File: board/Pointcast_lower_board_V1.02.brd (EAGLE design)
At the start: 100.3 x 80 mm, 29 parts, among them U6 Ethernet, X2 3G module, X4 3GS shield

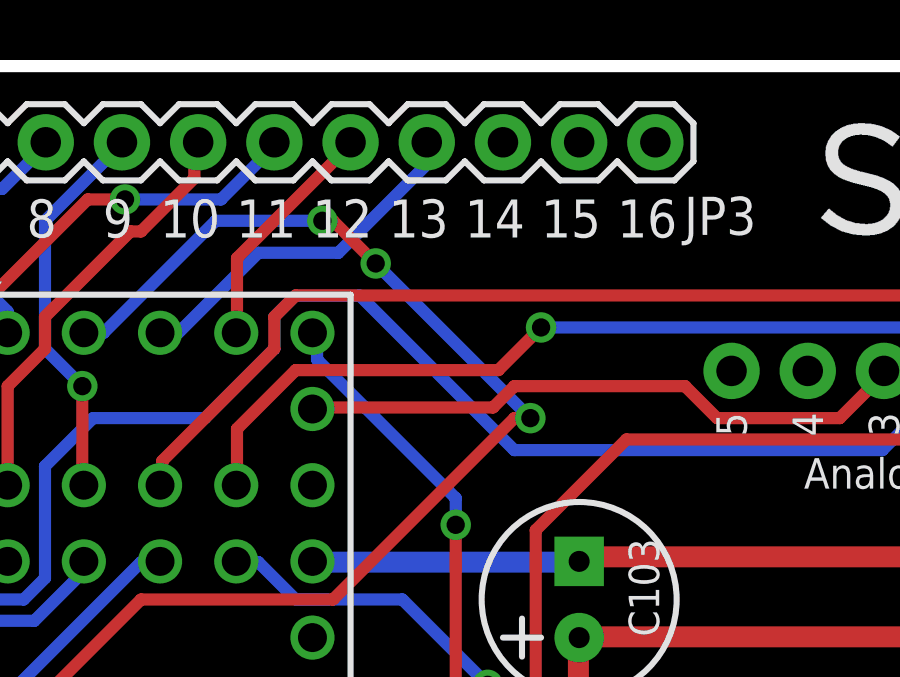
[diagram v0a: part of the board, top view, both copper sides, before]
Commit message: V3.7.8 added temperature on main screen, dev and api switch on display, logging header with logs, retarts and fails
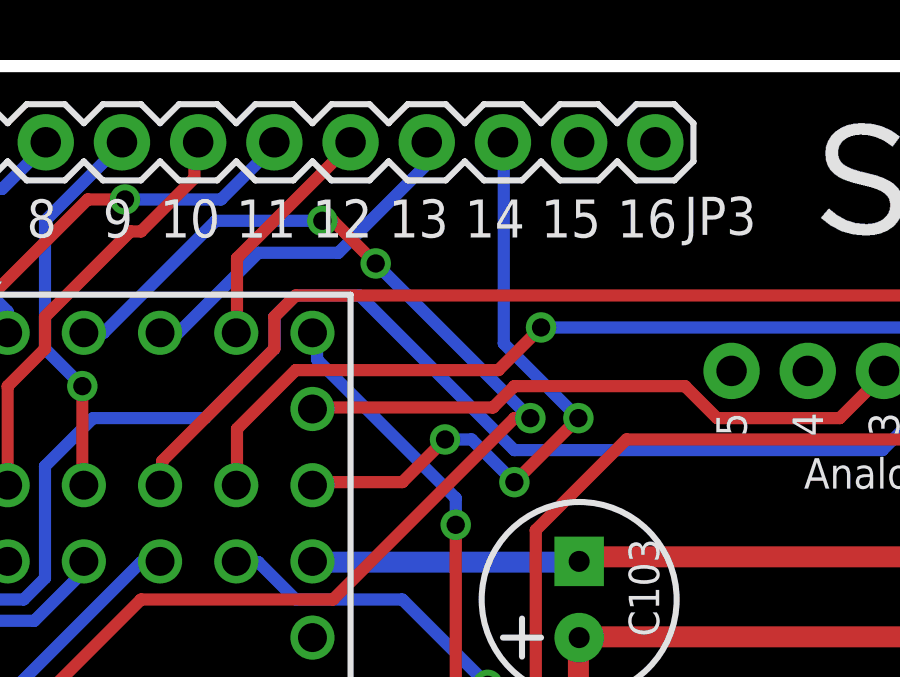
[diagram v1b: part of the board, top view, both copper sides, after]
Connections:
- new net N$22: JP3.14, TEENSY.PGM
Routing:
- net N$22: track 0.00 -> 21.2 mm, vias 0 -> 3
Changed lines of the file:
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@@
 <?xml version="1.0" encoding="utf-8"?>
 <!DOCTYPE eagle SYSTEM "eagle.dtd">
-<eagle version="7.2.0">
+<eagle version="7.5.0">
 <drawing>
 <settings>
@@
 <wire x1="7.8232" y1="75.2094" x2="7.860296875" y2="75.218390625" width="0.4064" layer="16"/>
 </signal>
+<signal name="N$22">
+<contactref element="JP3" pad="14"/>
+<contactref element="TEENSY" pad="PGM"/>
+<wire x1="39.8272" y1="66.1416" x2="36.9824" y2="66.1416" width="0.4064" layer="1"/>
+<wire x1="41.2496" y1="67.564" x2="39.8272" y2="66.1416" width="0.4064" layer="1"/>
+<wire x1="42.1386" y1="67.564" x2="41.2496" y2="67.564" width="0.4064" layer="16"/>
+<wire x1="43.561" y1="66.1416" x2="42.1386" y2="67.564" width="0.4064" layer="16"/>
+<wire x1="45.6946" y1="68.2752" x2="43.561" y2="66.1416" width="0.4064" layer="1"/>
+<wire x1="43.2054" y1="70.7644" x2="45.6946" y2="68.2752" width="0.4064" layer="16"/>
+<wire x1="43.2054" y1="77.343" x2="43.2054" y2="70.7644" width="0.4064" layer="16"/>
+<wire x1="36.9824" y1="66.1416" x2="36.83" y2="66.04" width="0.4064" layer="1"/>
+<wire x1="43.2054" y1="77.343" x2="43.18" y2="77.47" width="0.4064" layer="16"/>
+<via x="41.2496" y="67.564" extent="1-16" drill="0.6096"/>
+<via x="43.561" y="66.1416" extent="1-16" drill="0.6096"/>
+<via x="45.6946" y="68.2752" extent="1-16" drill="0.6096"/>
+</signal>
 </signals>
